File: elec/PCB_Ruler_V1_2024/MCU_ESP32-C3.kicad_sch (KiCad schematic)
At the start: 1 part, among them U2 ESP32-C3-WROOM-02-H4

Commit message: IMU
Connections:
- net GND: now reaches U2.19 (GND__1)
- net GND: now also U2.20 (GND__2), U2.21 (GND__3), U2.22 (GND__4), U2.23 (GND__5), U2.24 (GND__6), U2.25 (GND__7), U2.26 (GND__8), U2.27 (GND__9), U2.28 (GND__10), U2.29 (GND__11), U2.30 (GND__12), U2.31 (GND__13), U2.32 (GND__14), U2.33 (GND__15), U2.34 (GND__16), U2.35 (GND__17), U2.36 (GND__18), U2.37 (GND__19), U2.38 (GND__20), U2.39 (GND__21), U2.9 (GND)

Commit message: battery charger
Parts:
- added C4: 1uF, symbol Device:C
- added R2: 1M, symbol Device:R
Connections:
- net GND: now also C4.2
- net +3.3V: now reaches U2.1 (3V3)
- net +3.3V: now also C4.1
- net CS_Ecran: now reaches U2.10 (IO10)
- net USB_D-: now reaches U2.13 (IO18)
- net USB_D+: now reaches U2.14 (IO19)
- net SPI_CLK: now reaches U2.16 (IO2)
- net SPI_MOSI: now reaches U2.3 (IO4)

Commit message: Laser
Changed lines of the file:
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@@
+		)
+	)
+	(global_label "XSHUT"
+		(shape input)
+		(at 34.29 81.28 180)
+		(fields_autoplaced yes)
+		(effects
+			(font
+				(size 1.27 1.27)
+				(thickness 0.254)
+				(bold yes)
+			)
+			(justify right)
+		)
+		(property "Intersheetrefs" "${INTERSHEET_REFS}"
+			(at 24.7812 81.28 0)
+			(effects
+				(font
+					(size 1.27 1.27)
+				)
+				(justify right)
+				(hide yes)
+			)
 		)
 	)

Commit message: Almost finished schematic...
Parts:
- added J2: USB-C, Connector_USB:USB_C_Receptacle_G-Switch_GT-USB-7010ASV, symbol Connector:USB_C_Receptacle_USB2.0_16P
- added R10, R9: 5K1, symbol Device:R
- added R12: 10K, symbol Device:R
- added SW1, SW2: CS1213AGF260, CS1213AGF260:SW_CS1213AGF260_CRS, symbol CS1213AGF260:CS1213AGF260
- R2: value 1M -> 10K
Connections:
- net +3.3V: now also R2.2, R12.2
- net GND: now also J2.A1 (GND), J2.A12 (GND), J2.B1 (GND), J2.B12 (GND), J2.S1 (SHIELD), R10.2, R9.2, SW1.2, SW2.2
- net RESET_Ecran: now also U2.8 (IO9), R12.1, SW1.1
- net RS: now also U2.7 (IO8)
- net SCL: now also U2.15 (IO3)
- net SDA: now also U2.16 (IO2)
- net SPI_CLK: now also U2.3 (IO4); no longer U2.16 (IO2)
- net SPI_MOSI: now also U2.4 (IO5); no longer U2.3 (IO4)
- net Touch0: now also U2.18 (IO0)
- net Touch1: now also U2.17 (IO1)
- net USB_D+: now also J2.A6 (D+), J2.B6 (D+)
- net USB_D-: now also J2.A7 (D-), J2.B7 (D-)
- net EN: now reaches R2.1
- net EN: now also U2.2 (EN), SW2.1
- net SPI_MISO: now reaches U2.5 (IO6)
- net INT_IO_Extender: now reaches U2.6 (IO7)
- new net: J2.B5 (CC2), R9.1
- new net: J2.A5 (CC1), R10.1
- new net +5V: J2.A4 (VBUS), J2.A9 (VBUS), J2.B4 (VBUS), J2.B9 (VBUS)
- no-connect marks 0 -> 2
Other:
- note added: "BOOT/RESET ECRAN"
- note added: "RESET"
- note added: "USB-C"
- moved on the sheet: U2

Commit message: protection and Buttons
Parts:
- added D2, D3: D_Zener, Diode_SMD:D_SOD-923, symbol Device:D_Zener
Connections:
- net GND: now also D2.2 (A), D3.2 (A)
- net USB_D+: now also D3.1 (K)
- net USB_D-: now also D2.1 (K)
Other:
- moved on the sheet: R10, R9, U2

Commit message: started pcb
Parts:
- added C1: 1uF, Capacitor_SMD:C_0603_1608Metric_Pad1.08x0.95mm_HandSolder, symbol Device:C
- C2: renamed from C4; footprint (none) -> Capacitor_SMD:C_0603_1608Metric_Pad1.08x0.95mm_HandSolder
- R1: renamed from R12; footprint (none) -> Resistor_SMD:R_0603_1608Metric_Pad0.98x0.95mm_HandSolder
- R2: footprint (none) -> Resistor_SMD:R_0603_1608Metric_Pad0.98x0.95mm_HandSolder
- R3: renamed from R9; footprint (none) -> Resistor_SMD:R_0603_1608Metric_Pad0.98x0.95mm_HandSolder
- R4: renamed from R10; footprint (none) -> Resistor_SMD:R_0603_1608Metric_Pad0.98x0.95mm_HandSolder
- renumbered D2 to D1, D3 to D2, J2 to J1, U2 to U1
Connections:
- net SPI_MISO is gone; now on net SPI_CLK: U1.5 (IO6)
- net EN: now also C1.1
- net GND: now also C1.2
- net SPI_CLK: no longer U1.3 (IO4)
- new net Val_Bat: U1.3 (IO4)

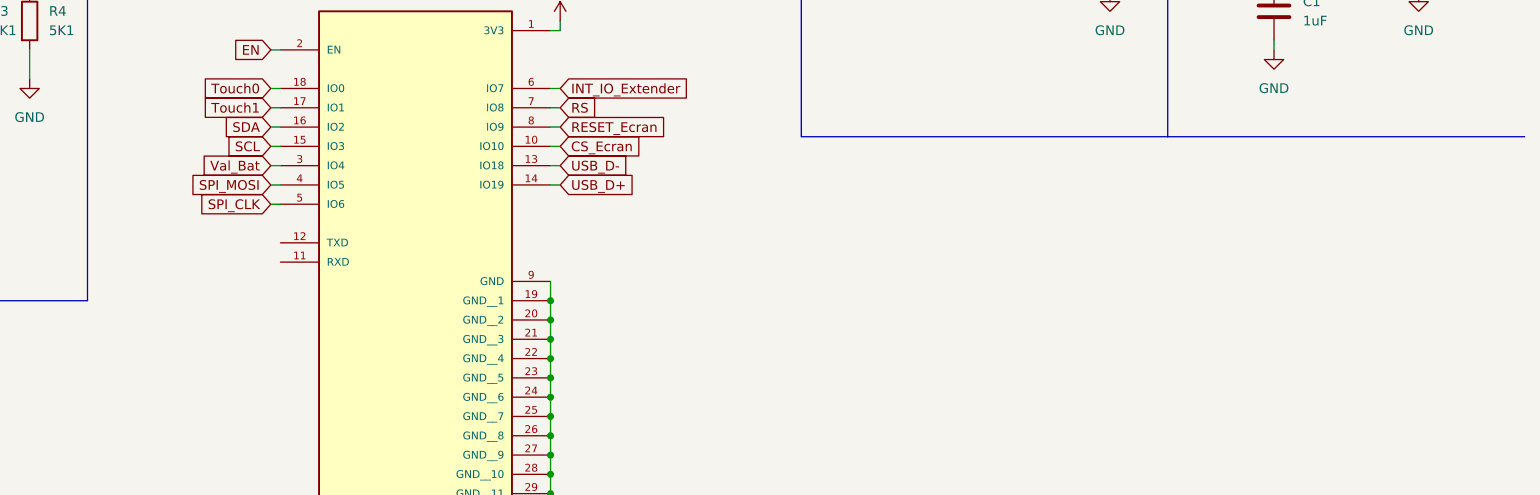
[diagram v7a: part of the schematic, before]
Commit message: Added to schematic what was missing
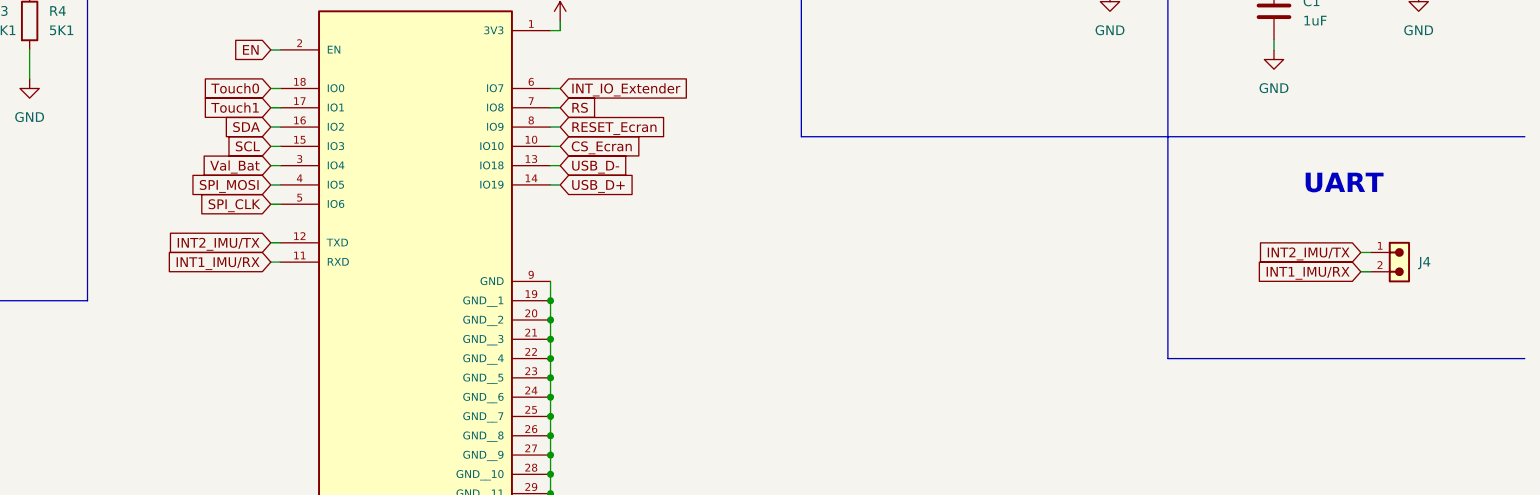
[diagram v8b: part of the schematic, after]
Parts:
- added J4: 61300211121, Header2_1:61300211121, symbol Header2_1:6130XX11121_61300211121
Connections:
- net INT1_IMU/RX: now reaches U1.11 (RXD)
- net INT1_IMU/RX: now also J4.2
- net INT2_IMU/TX: now reaches U1.12 (TXD)
- net INT2_IMU/TX: now also J4.1
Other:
- note added: "UART"
